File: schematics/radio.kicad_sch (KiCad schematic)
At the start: 24 parts, among them J4 BMI-S-201, U7 Si4463, U8 MAX-M8Q

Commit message: Complete revision 1 schematic
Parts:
- removed R11, R4: 10k, Strix:R_0402, symbol Strix:R
- renumbered C19 to C15, C20 to C16, C21 to C17, C22 to C18, C23 to C19, C24 to C20, C25 to C21, C26 to C22, C27 to C23, C28 to C24, C29 to C25, C30 to C26, J4 to J6
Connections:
- net RADIO_CLK_1.65V: no longer names the net of U7.17 (XIN)
- no-connect marks 14 -> 13
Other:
- note removed: "Drop XIN Voltage"
- moved on the sheet: C15, C16, C17, C18, C19, C20, C21, C22, C23, C24, C25, C26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

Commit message: Add oscillators and clean up schematics
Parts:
- added C?: 100n, Strix:C_0402, symbol Strix:C
- added C?: 2n, Strix:C_0402, symbol Strix:C
- added Y?: LFTCXO068373, Strix:LFTCXO068373, symbol Strix:LFTCXO068373
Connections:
- net GND: now also C?.2, Y?.1 (GND), Y?.2 (GND)
- net at U7.17 (XIN): now also C?.2
- net RADIO_MISO renamed MISO
- net RADIO_MOSI renamed MOSI
- net RADIO_SCLK renamed SCLK
- new net: C?.1, Y?.3 (OUT)
- new net 1v8: C?.1, Y?.4 (VCC)
- no-connect marks 13 -> 14
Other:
- note added: "Temperature-Compensated Crystal Oscillator"
- moved on the sheet: C15, C16, C17, C18, C19, C20, J6, U8

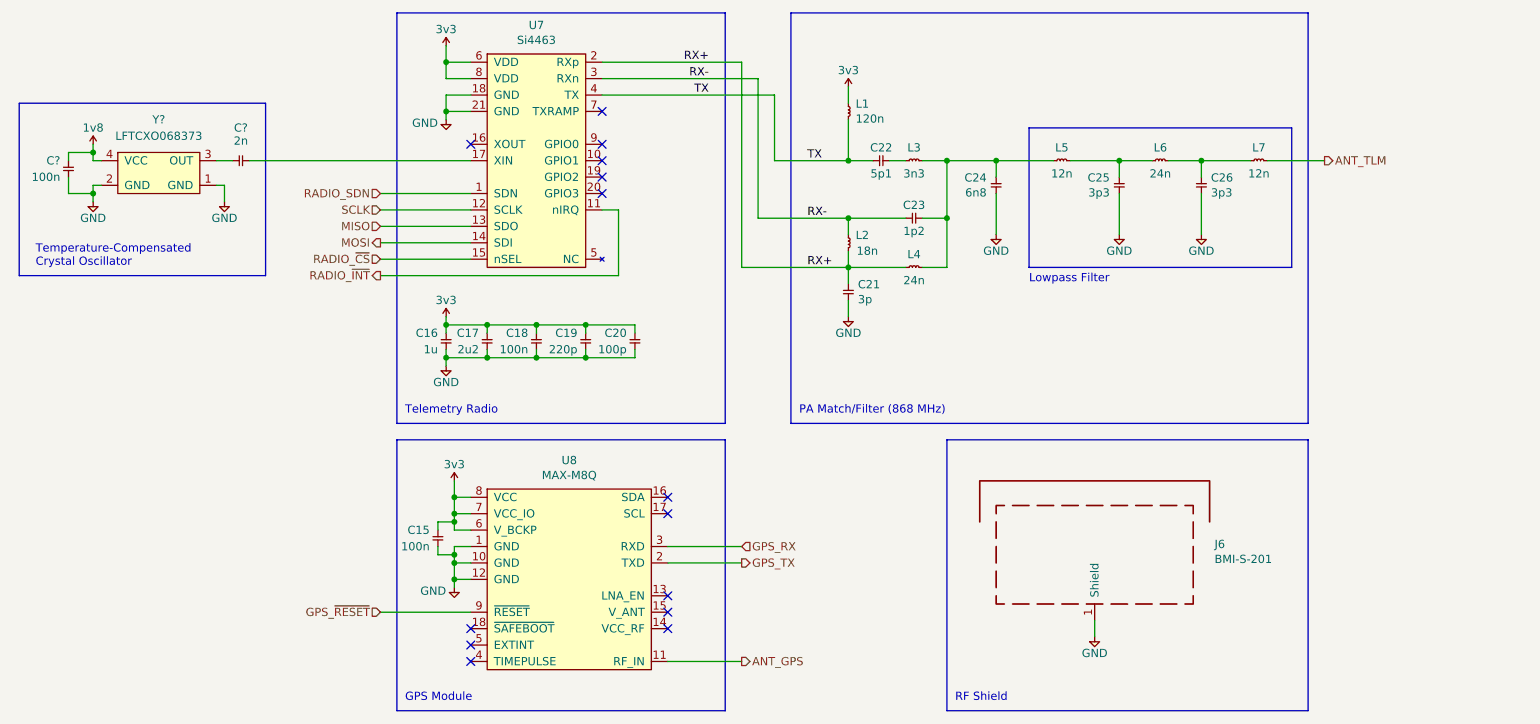
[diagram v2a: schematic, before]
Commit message: Add missing IC footprints
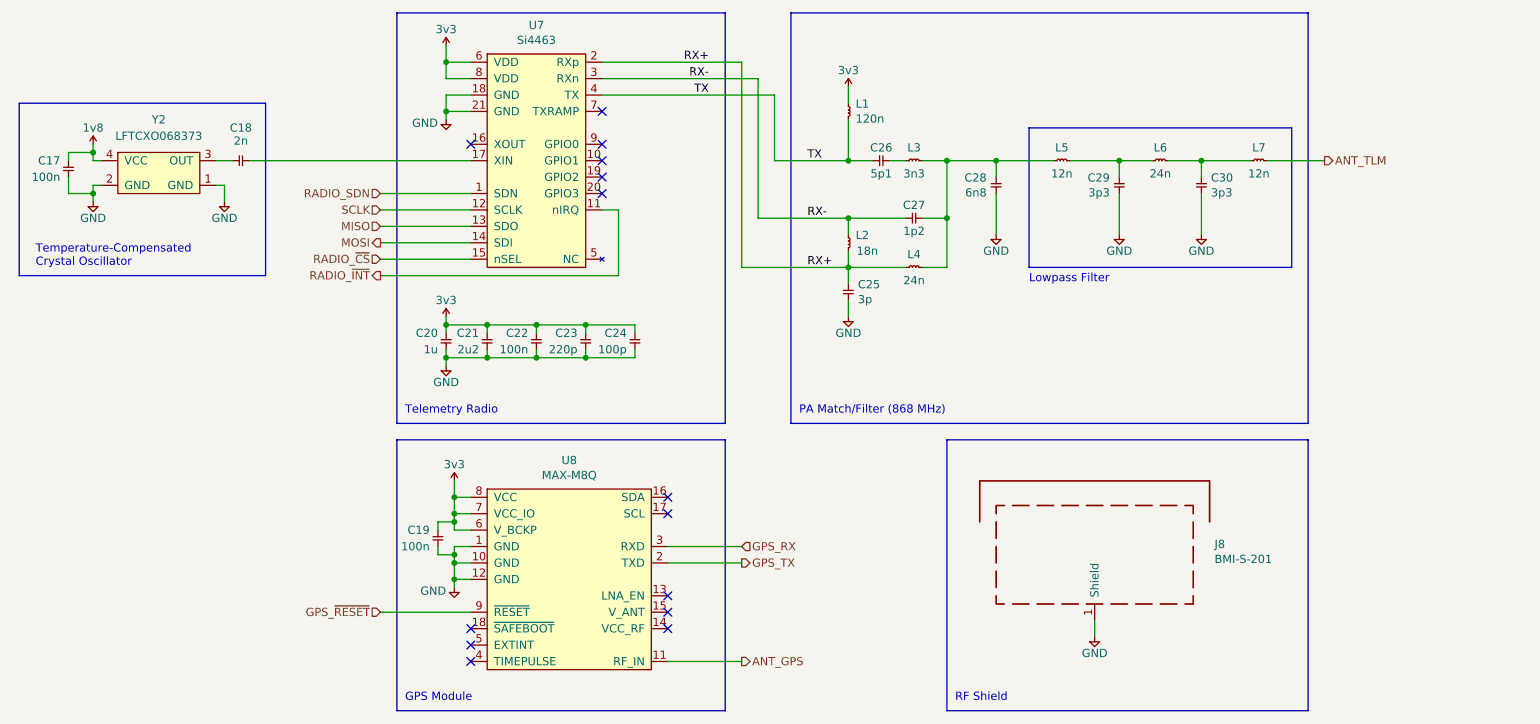
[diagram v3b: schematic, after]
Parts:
- gave numbers to parts that had none: 3
- renumbered C15 to C19, C16 to C20, C17 to C21, C18 to C22, C19 to C23, C20 to C24, C21 to C25, C22 to C26, C23 to C27, C24 to C28, C25 to C29, C26 to C30, J6 to J8
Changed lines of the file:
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@@
   (symbol (lib_id "Strix:GND") (at 92.71 62.23 0) (unit 1)
     (in_bom yes) (on_board yes)
-    (property "Reference" "#PWR031" (id 0) (at 89.408 61.214 0)
+    (property "Reference" "#PWR033" (id 0) (at 89.408 61.214 0)
       (effects (font (size 1.27 1.27)) (justify left) hide)
     )
@@
   (symbol (lib_id "Strix:3v3") (at 92.71 50.8 0) (unit 1)
     (in_bom yes) (on_board yes)
-    (property "Reference" "#PWR030" (id 0) (at 92.71 48.006 0)
+    (property "Reference" "#PWR032" (id 0) (at 92.71 48.006 0)
       (effects (font (size 1.27 1.27)) (justify left) hide)
     )
@@
   (symbol (lib_id "Strix:3v3") (at 92.71 92.71 0) (unit 1)
     (in_bom yes) (on_board yes)
-    (property "Reference" "#PWR032" (id 0) (at 92.71 89.916 0)
+    (property "Reference" "#PWR034" (id 0) (at 92.71 89.916 0)
       (effects (font (size 1.27 1.27)) (justify left) hide)
     )
@@
   (symbol (lib_id "Strix:GND") (at 92.71 100.33 0) (unit 1)
     (in_bom yes) (on_board yes)
-    (property "Reference" "#PWR033" (id 0) (at 89.408 99.314 0)
+    (property "Reference" "#PWR035" (id 0) (at 89.408 99.314 0)
       (effects (font (size 1.27 1.27)) (justify left) hide)
     )
@@
   (symbol (lib_id "Strix:C") (at 121.92 95.25 90) (mirror x) (unit 1)
     (in_bom yes) (on_board yes)
-    (property "Reference" "C20" (id 0) (at 120.65 95.25 90)
+    (property "Reference" "C24" (id 0) (at 120.65 95.25 90)
       (effects (font (size 1.27 1.27)) (justify left))
     )
@@
   (symbol (lib_id "Strix:C") (at 114.3 95.25 90) (mirror x) (unit 1)
     (in_bom yes) (on_board yes)
-    (property "Reference" "C19" (id 0) (at 113.03 95.25 90)
+    (property "Reference" "C23" (id 0) (at 113.03 95.25 90)
       (effects (font (size 1.27 1.27)) (justify left))
     )
@@
   (symbol (lib_id "Strix:C") (at 106.68 95.25 90) (mirror x) (unit 1)
     (in_bom yes) (on_board yes)
-    (property "Reference" "C18" (id 0) (at 105.41 95.25 90)
+    (property "Reference" "C22" (id 0) (at 105.41 95.25 90)
       (effects (font (size 1.27 1.27)) (justify left))
     )
@@
   (symbol (lib_id "Strix:C") (at 99.06 95.25 90) (mirror x) (unit 1)
     (in_bom yes) (on_board yes)
-    (property "Reference" "C17" (id 0) (at 97.79 95.25 90)
+    (property "Reference" "C21" (id 0) (at 97.79 95.25 90)
       (effects (font (size 1.27 1.27)) (justify left))
     )
@@
   (symbol (lib_id "Strix:C") (at 92.71 95.25 90) (mirror x) (unit 1)
     (in_bom yes) (on_board yes)
-    (property "Reference" "C16" (id 0) (at 91.44 95.25 90)
+    (property "Reference" "C20" (id 0) (at 91.44 95.25 90)
       (effects (font (size 1.27 1.27)) (justify left))
     )
@@
   (symbol (lib_id "Strix:GND") (at 93.98 134.62 0) (unit 1)
     (in_bom yes) (on_board yes)
-    (property "Reference" "#PWR029" (id 0) (at 90.678 133.604 0)
+    (property "Reference" "#PWR037" (id 0) (at 90.678 133.604 0)
       (effects (font (size 1.27 1.27)) (justify left) hide)
     )
@@
   (symbol (lib_id "Strix:3v3") (at 93.98 118.11 0) (unit 1)
     (in_bom yes) (on_board yes)
-    (property "Reference" "#PWR028" (id 0) (at 93.98 115.316 0)
+    (property "Reference" "#PWR036" (id 0) (at 93.98 115.316 0)
       (effects (font (size 1.27 1.27)) (justify left) hide)
     )
@@
   (symbol (lib_id "Strix:C") (at 91.44 128.27 90) (unit 1)
     (in_bom yes) (on_board yes)
-    (property "Reference" "C15" (id 0) (at 90.17 125.73 90)
+    (property "Reference" "C19" (id 0) (at 90.17 125.73 90)
       (effects (font (size 1.27 1.27)) (justify left))
     )
@@
   (symbol (lib_id "Strix:GND") (at 196.85 80.01 0) (unit 1)
     (in_bom yes) (on_board yes)
-    (property "Reference" "#PWR038" (id 0) (at 193.548 78.994 0)
+    (property "Reference" "#PWR042" (id 0) (at 193.548 78.994 0)
       (effects (font (size 1.27 1.27)) (justify left) hide)
     )
@@
   (symbol (lib_id "Strix:3v3") (at 154.94 57.15 0) (unit 1)
     (in_bom yes) (on_board yes)
-    (property "Reference" "#PWR034" (id 0) (at 154.94 54.356 0)
+    (property "Reference" "#PWR038" (id 0) (at 154.94 54.356 0)
       (effects (font (size 1.27 1.27)) (justify left) hide)
     )
@@
   (symbol (lib_id "Strix:C") (at 163.83 77.47 0) (unit 1)
     (in_bom yes) (on_board yes)
-    (property "Reference" "C23" (id 0) (at 165.1 76.2 0)
+    (property "Reference" "C27" (id 0) (at 165.1 76.2 0)
       (effects (font (size 1.27 1.27)) (justify bottom))
     )
@@
   (symbol (lib_id "Strix:GND") (at 154.94 92.71 0) (unit 1)
     (in_bom yes) (on_board yes)
-    (property "Reference" "#PWR035" (id 0) (at 151.638 91.694 0)
+    (property "Reference" "#PWR039" (id 0) (at 151.638 91.694 0)
       (effects (font (size 1.27 1.27)) (justify left) hide)
     )
@@
   (symbol (lib_id "Strix:C") (at 154.94 87.63 270) (unit 1)
     (in_bom yes) (on_board yes)
-    (property "Reference" "C21" (id 0) (at 156.4132 87.7316 90)
+    (property "Reference" "C25" (id 0) (at 156.4132 87.7316 90)
       (effects (font (size 1.27 1.27)) (justify left))
     )
@@
   (symbol (lib_id "Strix:C") (at 196.85 71.12 90) (mirror x) (unit 1)
     (in_bom yes) (on_board yes)
-    (property "Reference" "C25" (id 0) (at 195.3768 71.2216 90)
+    (property "Reference" "C29" (id 0) (at 195.3768 71.2216 90)
       (effects (font (size 1.27 1.27)) (justify left))
     )
@@
   (symbol (lib_id "Strix:C") (at 209.55 71.12 270) (unit 1)
     (in_bom yes) (on_board yes)
-    (property "Reference" "C26" (id 0) (at 211.0232 71.2216 90)
+    (property "Reference" "C30" (id 0) (at 211.0232 71.2216 90)
       (effects (font (size 1.27 1.27)) (justify left))
     )
@@
   (symbol (lib_id "Strix:C") (at 158.75 68.58 0) (unit 1)
     (in_bom yes) (on_board yes)
-    (property "Reference" "C22" (id 0) (at 160.02 67.31 0)
+    (property "Reference" "C26" (id 0) (at 160.02 67.31 0)
       (effects (font (size 1.27 1.27)) (justify bottom))
     )
@@
   (symbol (lib_id "Strix:C") (at 177.8 71.12 90) (mirror x) (unit 1)
     (in_bom yes) (on_board yes)
-    (property "Reference" "C24" (id 0) (at 176.3268 71.2216 90)
+    (property "Reference" "C28" (id 0) (at 176.3268 71.2216 90)
       (effects (font (size 1.27 1.27)) (justify left))
     )
@@
   (symbol (lib_id "Strix:GND") (at 177.8 80.01 0) (unit 1)
     (in_bom yes) (on_board yes)
-    (property "Reference" "#PWR036" (id 0) (at 174.498 78.994 0)
+    (property "Reference" "#PWR040" (id 0) (at 174.498 78.994 0)
       (effects (font (size 1.27 1.27)) (justify left) hide)
     )
@@
   (symbol (lib_id "Strix:GND") (at 209.55 80.01 0) (unit 1)
     (in_bom yes) (on_board yes)
-    (property "Reference" "#PWR039" (id 0) (at 206.248 78.994 0)
+    (property "Reference" "#PWR043" (id 0) (at 206.248 78.994 0)
       (effects (font (size 1.27 1.27)) (justify left) hide)
     )
@@
   (symbol (lib_id "Strix:GND") (at 193.04 142.24 0) (unit 1)
     (in_bom yes) (on_board yes)
-    (property "Reference" "#PWR037" (id 0) (at 189.738 141.224 0)
+    (property "Reference" "#PWR041" (id 0) (at 189.738 141.224 0)
       (effects (font (size 1.27 1.27)) (justify left) hide)
     )
@@
   (symbol (lib_id "Strix:BMI-S-201") (at 193.04 129.54 0) (unit 1)
     (in_bom yes) (on_board yes)
-    (property "Reference" "J6" (id 0) (at 211.582 127.9144 0)
+    (property "Reference" "J8" (id 0) (at 211.582 127.9144 0)
       (effects (font (size 1.27 1.27)) (justify left))
     )
@@
   (symbol (lib_id "Strix:GND") (at 38.1 74.93 0) (unit 1)
     (in_bom yes) (on_board yes)
-    (property "Reference" "#PWR?" (id 0) (at 34.798 73.914 0)
+    (property "Reference" "#PWR030" (id 0) (at 34.798 73.914 0)
       (effects (font (size 1.27 1.27)) (justify left) hide)
     )
@@
   (symbol (lib_id "Strix:C") (at 34.29 68.58 270) (unit 1)
     (in_bom yes) (on_board yes)
-    (property "Reference" "C?" (id 0) (at 33.02 68.58 90)
+    (property "Reference" "C17" (id 0) (at 33.02 68.58 90)
       (effects (font (size 1.27 1.27)) (justify right))
     )
@@
   (symbol (lib_id "Strix:1v8") (at 38.1 66.04 0) (unit 1)
     (in_bom yes) (on_board yes)
-    (property "Reference" "#PWR?" (id 0) (at 38.1 63.246 0)
+    (property "Reference" "#PWR029" (id 0) (at 38.1 63.246 0)
       (effects (font (size 1.27 1.27)) (justify left) hide)
     )
@@
   (symbol (lib_id "Strix:GND") (at 58.42 74.93 0) (unit 1)
     (in_bom yes) (on_board yes)
-    (property "Reference" "#PWR?" (id 0) (at 55.118 73.914 0)
+    (property "Reference" "#PWR031" (id 0) (at 55.118 73.914 0)
       (effects (font (size 1.27 1.27)) (justify left) hide)
     )
@@
   (symbol (lib_id "Strix:C") (at 59.69 68.58 0) (unit 1)
     (in_bom yes) (on_board yes)
-    (property "Reference" "C?" (id 0) (at 60.96 63.5 0))
+    (property "Reference" "C18" (id 0) (at 60.96 63.5 0))
     (property "Value" "2n" (id 1) (at 60.96 64.77 0)
       (effects (font (size 1.27 1.27)) (justify top))
@@
   (symbol (lib_id "Strix:LFTCXO068373") (at 48.26 69.85 0) (unit 1)
     (in_bom yes) (on_board yes) (fields_autoplaced)
-    (property "Reference" "Y?" (id 0) (at 48.26 62.23 0))
+    (property "Reference" "Y2" (id 0) (at 48.26 62.23 0))
     (property "Value" "LFTCXO068373" (id 1) (at 48.26 64.77 0))
     (property "Footprint" "Strix:LFTCXO068373" (id 2) (at 43.18 68.58 0)

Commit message: Rough power and RF layouts
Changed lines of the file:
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@@
     (stroke (width 0) (type default) (color 0 0 0 0))
   )
-  (wire (pts (xy 143.51 58.42) (xy 143.51 68.58))
+  (wire (pts (xy 138.43 58.42) (xy 138.43 68.58))
     (stroke (width 0) (type default) (color 0 0 0 0))
   )
@@
     (stroke (width 0) (type default) (color 0 0 0 0))
   )
-  (wire (pts (xy 116.84 58.42) (xy 143.51 58.42))
+  (wire (pts (xy 116.84 58.42) (xy 138.43 58.42))
     (stroke (width 0) (type default) (color 0 0 0 0))
   )
@@
     (stroke (width 0) (type default) (color 0 0 0 0))
   )
+  (wire (pts (xy 143.51 53.34) (xy 143.51 85.09))
+    (stroke (width 0) (type default) (color 0 0 0 0))
+  )
   (wire (pts (xy 91.44 129.54) (xy 93.98 129.54))
     (stroke (width 0) (type default) (color 0 0 0 0))
@@
     (stroke (width 0) (type default) (color 0 0 0 0))
   )
-  (wire (pts (xy 116.84 53.34) (xy 138.43 53.34))
+  (wire (pts (xy 116.84 53.34) (xy 143.51 53.34))
     (stroke (width 0) (type default) (color 0 0 0 0))
   )
@@
     (stroke (width 0) (type default) (color 0 0 0 0))
   )
-  (wire (pts (xy 138.43 85.09) (xy 138.43 53.34))
-    (stroke (width 0) (type default) (color 0 0 0 0))
-  )
   (wire (pts (xy 93.98 118.11) (xy 93.98 120.65))
     (stroke (width 0) (type default) (color 0 0 0 0))
   )
-  (wire (pts (xy 143.51 68.58) (xy 154.94 68.58))
+  (wire (pts (xy 138.43 68.58) (xy 154.94 68.58))
     (stroke (width 0) (type default) (color 0 0 0 0))
   )
@@
     (stroke (width 0) (type default) (color 0 0 0 0))
   )
+  (wire (pts (xy 140.97 55.88) (xy 140.97 77.47))
+    (stroke (width 0) (type default) (color 0 0 0 0))
+  )
   (wire (pts (xy 82.55 81.28) (xy 96.52 81.28))
     (stroke (width 0) (type default) (color 0 0 0 0))
@@
     (stroke (width 0) (type default) (color 0 0 0 0))
   )
-  (wire (pts (xy 140.97 77.47) (xy 140.97 55.88))
-    (stroke (width 0) (type default) (color 0 0 0 0))
-  )
   (wire (pts (xy 92.71 60.96) (xy 92.71 62.23))
     (stroke (width 0) (type default) (color 0 0 0 0))
@@
     (stroke (width 0) (type default) (color 0 0 0 0))
   )
-  (wire (pts (xy 138.43 85.09) (xy 154.94 85.09))
-    (stroke (width 0) (type default) (color 0 0 0 0))
-  )
   (wire (pts (xy 34.29 73.66) (xy 38.1 73.66))
     (stroke (width 0) (type default) (color 0 0 0 0))
@@
     (stroke (width 0) (type default) (color 0 0 0 0))
   )
+  (wire (pts (xy 143.51 85.09) (xy 154.94 85.09))
+    (stroke (width 0) (type default) (color 0 0 0 0))
+  )
   (polyline (pts (xy 146.05 109.22) (xy 146.05 45.72))
     (stroke (width 0) (type default) (color 0 0 0 0))
@@
     (effects (font (size 1.27 1.27)) (justify left bottom))
   )
-  (label "TX" (at 133.35 58.42 180)
-    (effects (font (size 1.27 1.27)) (justify right bottom))
+  (label "TX" (at 129.54 58.42 0)
+    (effects (font (size 1.27 1.27)) (justify left bottom))
   )
   (label "RX-" (at 148.59 77.47 0)
     (effects (font (size 1.27 1.27)) (justify left bottom))
   )
-  (label "RX-" (at 133.35 55.88 180)
-    (effects (font (size 1.27 1.27)) (justify right bottom))
-  )
-  (label "RX+" (at 133.35 53.34 180)
-    (effects (font (size 1.27 1.27)) (justify right bottom))
+  (label "RX-" (at 129.54 55.88 0)
+    (effects (font (size 1.27 1.27)) (justify left bottom))
+  )
+  (label "RX+" (at 129.54 53.34 0)
+    (effects (font (size 1.27 1.27)) (justify left bottom))
   )
   (hierarchical_label "GPS_RX" (shape input) (at 138.43 128.27 0)
